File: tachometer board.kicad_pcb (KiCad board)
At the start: 2 copper layers, 22.4 x 13.5 mm, 5 parts, among them J1 Conn_01x04

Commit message: Update silkscreen and export gerbers
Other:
- board text added: "3.3VIN"
- board text added: "GND"
- board text added: "Nerf Tachometer Version 1.0 Designed by Mark Ghebrial"
- board text added: "OUT1"
- board text added: "OUT2"
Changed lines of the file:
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@@
     (descr "JST PH series connector, S4B-PH-K (http://www.jst-mfg.com/product/pdf/eng/ePH.pdf), generated with kicad-footprint-generator")
     (tags "connector JST PH top entry")
-    (property "Sheetfile" "protean board.kicad_sch")
+    (property "Sheetfile" "tachometer board.kicad_sch")
     (property "Sheetname" "")
     (property "ki_description" "Generic connector, single row, 01x04, script generated (kicad-library-utils/schlib/autogen/connector/)")
     (property "ki_keywords" "connector")
     (attr through_hole)
-    (fp_text reference "J1" (at 3 -2.55 180) (layer "F.SilkS")
+    (fp_text reference "J1" (at 3 -2.55 180) (layer "F.SilkS") hide
         (effects (font (size 1 1) (thickness 0.15)))
     )
@@
   (footprint "Marks Library:ITR20001-T" (layer "F.Cu")
     (at 164.067893 111.7 -90)
-    (property "Sheetfile" "protean board.kicad_sch")
+    (property "Sheetfile" "tachometer board.kicad_sch")
     (property "Sheetname" "")
     (attr through_hole)
@@
     (descr "Resistor SMD 1210 (3225 Metric), square (rectangular) end terminal, IPC_7351 nominal with elongated pad for handsoldering. (Body size source: IPC-SM-782 page 72, https://www.pcb-3d.com/wordpress/wp-content/uploads/ipc-sm-782a_amendment_1_and_2.pdf), generated with kicad-footprint-generator")
     (tags "resistor handsolder")
-    (property "Sheetfile" "protean board.kicad_sch")
+    (property "Sheetfile" "tachometer board.kicad_sch")
     (property "Sheetname" "")
     (property "ki_description" "Resistor")
@@
     (descr "Resistor SMD 1210 (3225 Metric), square (rectangular) end terminal, IPC_7351 nominal with elongated pad for handsoldering. (Body size source: IPC-SM-782 page 72, https://www.pcb-3d.com/wordpress/wp-content/uploads/ipc-sm-782a_amendment_1_and_2.pdf), generated with kicad-footprint-generator")
     (tags "resistor handsolder")
-    (property "Sheetfile" "protean board.kicad_sch")
+    (property "Sheetfile" "tachometer board.kicad_sch")
     (property "Sheetname" "")
     (property "ki_description" "Resistor")
@@
   (footprint "Marks Library:ITR20001-T" (layer "F.Cu")
     (at 148.317893 111.7 90)
-    (property "Sheetfile" "protean board.kicad_sch")
+    (property "Sheetfile" "tachometer board.kicad_sch")
     (property "Sheetname" "")
     (attr through_hole)
@@
   (gr_line (start 167.367893 114.242893) (end 167.367893 109.142893)
     (stroke (width 0.1) (type solid)) (layer "Edge.Cuts"))
+  (gr_text "3.3VIN" (at 159.85 101.19762 90) (layer "B.SilkS")
+    (effects (font (size 1 1) (thickness 0.15)) (justify left bottom mirror))
+  )
+  (gr_text "OUT2" (at 155.85 102.15 90) (layer "B.SilkS")
+    (effects (font (size 1 1) (thickness 0.15)) (justify left bottom mirror))
+  )
+  (gr_text "GND" (at 157.85 102.911905 90) (layer "B.SilkS")
+    (effects (font (size 1 1) (thickness 0.15)) (justify left bottom mirror))
+  )
+  (gr_text "Nerf Tachometer\nVersion 1.0\nDesigned by\nMark Ghebrial" (at 151.45 109.1 180) (layer "B.SilkS")
+    (effects (font (size 0.75 0.75) (thickness 0.15)) (justify left bottom mirror))
+  )
+  (gr_text "OUT1" (at 153.9 102.15 90) (layer "B.SilkS")
+    (effects (font (size 1 1) (thickness 0.15)) (justify left bottom mirror))
+  )
   (segment (start 159.192893 109.820711) (end 159.192893 107.15) (width 0.25) (layer "F.Cu") (net 1))
   (segment (start 154.934314 113.25) (end 153.4 113.25) (width 0.25) (layer "F.Cu") (net 1))

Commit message: Add README.md
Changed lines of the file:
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@@
       (outputformat 1)
       (mirror false)
-      (drillshape 1)
+      (drillshape 0)
       (scaleselection 1)
-      (outputdirectory "")
+      (outputdirectory "gerbers/")
     )
   )
@@
     (fp_line (start 7.95 6.25) (end 7.95 -1.35)
       (stroke (width 0.1) (type solid)) (layer "F.Fab"))
-    (pad "1" thru_hole roundrect (at 0 0 180) (size 1.2 1.75) (drill 0.75) (layers "*.Cu" "*.Mask") (roundrect_rratio 0.208333)
+    (pad "1" thru_hole roundrect (at 0 0 180) (size 1.2 1.75) (drill 0.75) (layers "*.Cu" "*.Mask") (roundrect_rratio 0.2083333333)
       (net 1 "+3.3V") (pinfunction "Pin_1") (pintype "passive"))
     (pad "2" thru_hole oval (at 2 0 180) (size 1.2 1.75) (drill 0.75) (layers "*.Cu" "*.Mask")
@@
     (fp_line (start 1.6 1.245) (end -1.6 1.245)
       (stroke (width 0.1) (type solid)) (layer "F.Fab"))
-    (pad "1" smd roundrect (at -1.55 0 90) (size 1.3 2.65) (layers "F.Cu" "F.Paste" "F.Mask") (roundrect_rratio 0.192308)
+    (pad "1" smd roundrect (at -1.55 0 90) (size 1.3 2.65) (layers "F.Cu" "F.Paste" "F.Mask") (roundrect_rratio 0.1923076923)
       (net 6 "Net-(U2-LED_VIN)") (pintype "passive"))
-    (pad "2" smd roundrect (at 1.55 0 90) (size 1.3 2.65) (layers "F.Cu" "F.Paste" "F.Mask") (roundrect_rratio 0.192308)
+    (pad "2" smd roundrect (at 1.55 0 90) (size 1.3 2.65) (layers "F.Cu" "F.Paste" "F.Mask") (roundrect_rratio 0.1923076923)
       (net 1 "+3.3V") (pintype "passive"))
     (model "${KICAD6_3DMODEL_DIR}/Resistor_SMD.3dshapes/R_1210_3225Metric.wrl"
@@
     (fp_line (start 1.6 1.245) (end -1.6 1.245)
       (stroke (width 0.1) (type solid)) (layer "F.Fab"))
-    (pad "1" smd roundrect (at -1.55 0 270) (size 1.3 2.65) (layers "F.Cu" "F.Paste" "F.Mask") (roundrect_rratio 0.192308)
+    (pad "1" smd roundrect (at -1.55 0 270) (size 1.3 2.65) (layers "F.Cu" "F.Paste" "F.Mask") (roundrect_rratio 0.1923076923)
       (net 5 "Net-(U1-LED_VIN)") (pintype "passive"))
-    (pad "2" smd roundrect (at 1.55 0 270) (size 1.3 2.65) (layers "F.Cu" "F.Paste" "F.Mask") (roundrect_rratio 0.192308)
+    (pad "2" smd roundrect (at 1.55 0 270) (size 1.3 2.65) (layers "F.Cu" "F.Paste" "F.Mask") (roundrect_rratio 0.1923076923)
       (net 1 "+3.3V") (pintype "passive"))
     (model "${KICAD6_3DMODEL_DIR}/Resistor_SMD.3dshapes/R_1210_3225Metric.wrl"
@@
     (effects (font (size 1 1) (thickness 0.15)) (justify left bottom mirror))
   )
-  (gr_text "Nerf Tachometer\nVersion 1.0\nDesigned by\nMark Ghebrial" (at 151.45 109.1 180) (layer "B.SilkS")
-    (effects (font (size 0.75 0.75) (thickness 0.15)) (justify left bottom mirror))
-  )
-  (gr_text "OUT1" (at 153.9 102.15 90) (layer "B.SilkS")
+  (gr_text "Nerf Tachometer\nVersion 1.0\nDesigned by\nMark Ghebrial" (at 151.45 108.8 180) (layer "B.SilkS")
+    (effects (font (size 0.8 0.75) (thickness 0.15)) (justify left bottom mirror))
+  )
+  (gr_text "OUT1" (at 153.85 102.15 90) (layer "B.SilkS")
     (effects (font (size 1 1) (thickness 0.15)) (justify left bottom mirror))
   )

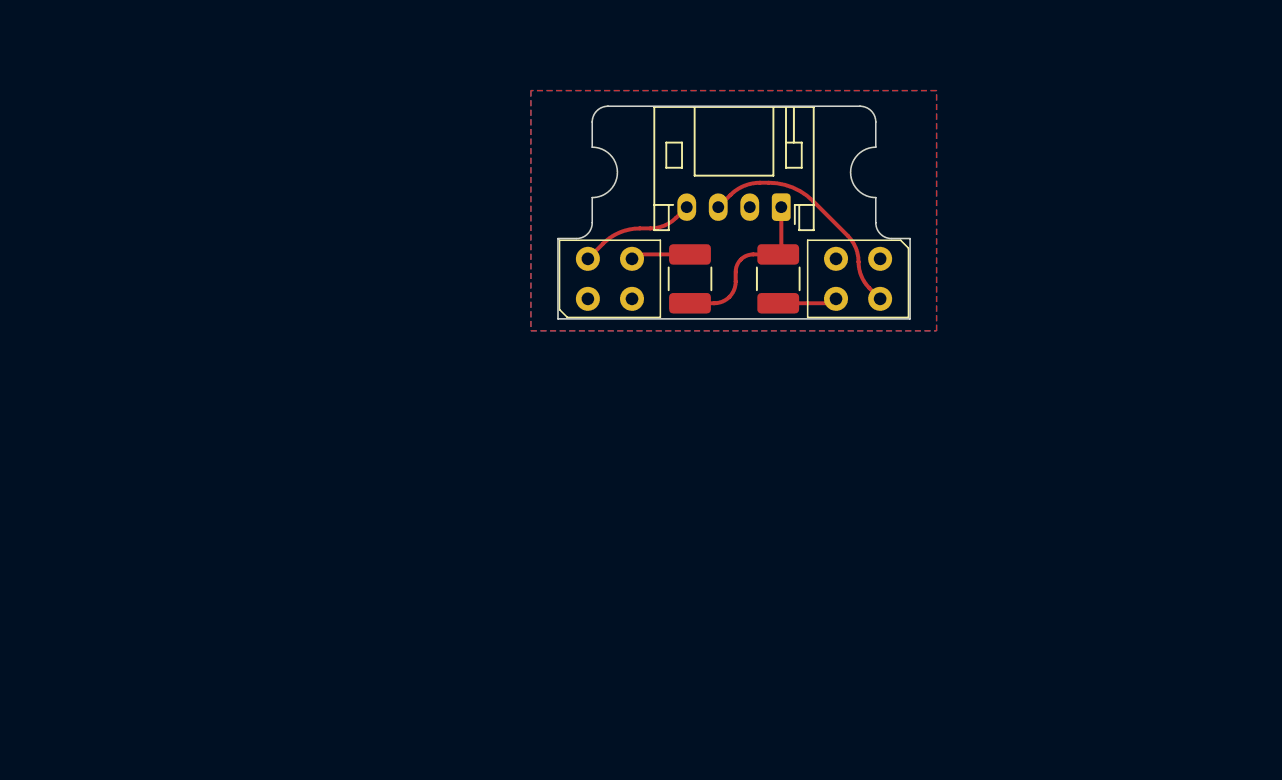
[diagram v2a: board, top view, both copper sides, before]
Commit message: Add SAMD MCU and MOSFET
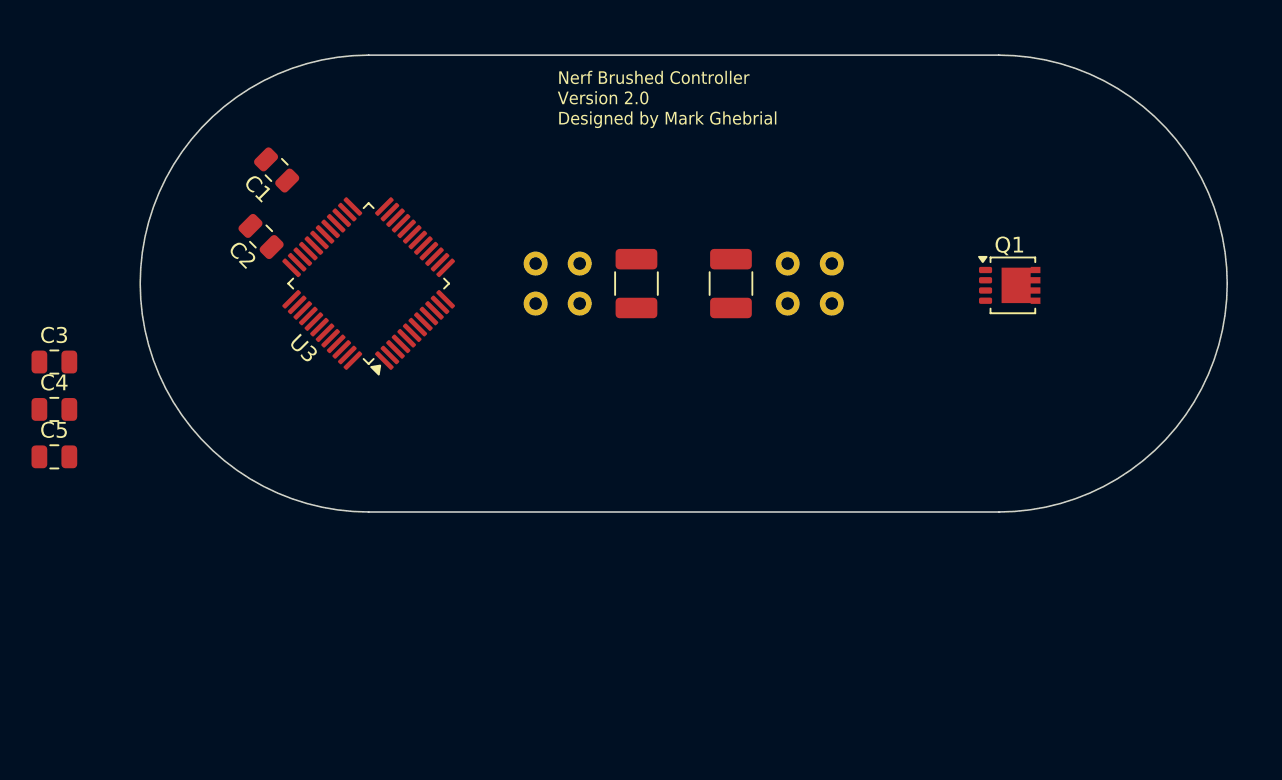
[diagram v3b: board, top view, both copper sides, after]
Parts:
- removed J1: Conn_01x04, Connector_JST:JST_PH_S4B-PH-K_1x04_P2.00mm_Horizontal
- added C1: C, Capacitor_SMD:C_0805_2012Metric, F.Cu at (127.2, 104.8)
- added C2: C, Capacitor_SMD:C_0805_2012Metric, F.Cu at (126.2, 109.0)
- added C3: C, Capacitor_SMD:C_0805_2012Metric, F.Cu at (113.0, 117.0)
- added C4: C, Capacitor_SMD:C_0805_2012Metric, F.Cu at (113.0, 120.0)
- added C5: C, Capacitor_SMD:C_0805_2012Metric, F.Cu at (113.0, 123.0)
- added Q1: PSMN8R5-40MSDX, Package_TO_SOT_SMD:LFPAK33, F.Cu at (173.7, 112.1)
- added U3: ATSAMD21G18A-A, Package_QFP:TQFP-48_7x7mm_P0.5mm, F.Cu at (133.0, 112.0)
- U1, U2: moved to B.Cu
- moved U2 19.1 mm to (145.0, 112.0)
- moved U1 12.7 mm to (161.0, 112.0)
- moved R1 3.41 mm to (150.0, 112.0)
- moved R2 3.01 mm to (156.0, 112.0)
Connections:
- U1 pad 4: /OUT1 -> /TACHA
- U2 pad 4: /OUT2 -> /TACHB
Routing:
- net /OUT2: track 14.6 -> 0.00 mm
- net +3.3V: track 10.7 -> 0.00 mm
- net /OUT1: track 7.36 -> 0.00 mm
- net Net-(U1-LED_VIN): track 3.78 -> 0.00 mm
- net Net-(U2-LED_VIN): track 3.76 -> 0.00 mm
- removed copper zone on B.Cu, net GND
- removed copper zone on F.Cu, net GND
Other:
- board size 22.4 x 13.5 mm -> 69 x 29 mm
- board text added: "Nerf Brushed Controller Version 2.0 Designed by Mark Ghebrial"
- board text removed: "3.3VIN"
- board text removed: "GND"
- board text removed: "Nerf Tachometer Version 1.0 Designed by Mark Ghebrial"
- board text removed: "OUT1"
- board text removed: "OUT2"

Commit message: Misc. changes to schematic and PCB
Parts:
- added J1: USB_B_Micro, Connector_USB:USB_Micro-B_Molex_47346-0001, F.Cu at (137.0, 100.5)
- added J2: Conn_01x05_Pin, Marks Library:4mm_by_6mm_Solder_Pad_x5, F.Cu at (165.0, 138.5)
- added Q2: PSMN8R5-40MSX, Package_TO_SOT_SMD:LFPAK33, F.Cu at (144.3, 133.2)
- added REF**: AMASS_XT30PW-F_1x02_P2.50mm_Horizontal, Connector_AMASS:AMASS_XT30PW-F_1x02_P2.50mm_Horizontal, B.Cu at (173.2, 107.5)
- added REF**: AMASS_XT30PW-M_1x02_P2.50mm_Horizontal, Connector_AMASS:AMASS_XT30PW-M_1x02_P2.50mm_Horizontal, B.Cu at (156.0, 116.8)
- added REF**: AMASS_XT30PW-F_1x02_P2.50mm_Horizontal, Connector_AMASS:AMASS_XT30PW-F_1x02_P2.50mm_Horizontal, B.Cu at (173.2, 121.2)
- added U4: ZXGD3009DY, Package_TO_SOT_SMD:SOT-23-6, F.Cu at (153.2, 133.2)
- added U5: ZXGD3009DY, Package_TO_SOT_SMD:SOT-23-6, F.Cu at (148.8, 133.2)
- added U6: AP2112K-3.3, Package_TO_SOT_SMD:SOT-23-5, F.Cu at (146.4, 105.5)
- C1, C2, C3, C4: footprint Capacitor_SMD:C_0805_2012Metric -> Capacitor_SMD:C_0402_1005Metric
- C5: value C -> 1uF; footprint Capacitor_SMD:C_0805_2012Metric -> Capacitor_SMD:C_0402_1005Metric
- Q1: value PSMN8R5-40MSDX -> PSMN8R5-40MSX
- moved Q1 26.5 mm to (157.7, 133.2)
- moved C5 19.2 mm to (126.6, 109.3), turned to 135 degrees
- moved C4 18.8 mm to (127.8, 108.2), turned to 135 degrees
- moved C3 18.5 mm to (128.8, 107.2), turned to 135 degrees
- moved C1 12.8 mm to (126.3, 117.6)
- moved C2 7.22 mm to (128.0, 116.0)
- moved R1 6.00 mm to (156.0, 112.0)
- moved R2 6.00 mm to (150.0, 112.0)
- turned U3 to 45 degrees
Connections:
- C5 pad 1: +3V3 -> Net-(U3-VDDCORE)
- Q1 pad 1: Net-(Q1-S-Pad1) -> GND
- Q1 pad 2: Net-(Q1-S-Pad1) -> GND
- Q1 pad 3: Net-(Q1-S-Pad1) -> GND
- Q1 pad 4: unconnected-(Q1-G-Pad4) -> /GATEA
- Q1 pad 5: unconnected-(Q1-D-Pad5) -> MOTORA-
- U1 pad 4: /TACHA -> TACHA
- U2 pad 4: /TACHB -> TACHB
- U3 pad 18: Net-(U3-GND-Pad18) -> GND
- U3 pad 25: unconnected-(U3-PA16-Pad25) -> TACHB
- U3 pad 26: unconnected-(U3-PA17-Pad26) -> TACHA
- U3 pad 33: unconnected-(U3-PA24-Pad33) -> USB_D-
- U3 pad 34: unconnected-(U3-PA25-Pad34) -> USB_D+
- U3 pad 35: Net-(U3-GND-Pad18) -> GND
- U3 pad 40: unconnected-(U3-~{RESET}-Pad40) -> RESET
- U3 pad 42: Net-(U3-GND-Pad18) -> GND
- U3 pad 43: +3V3 -> Net-(U3-VDDCORE)
- U3 pad 5: unconnected-(U3-GNDANA-Pad5) -> GND
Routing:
- net TACHA: track 0.00 -> 26.4 mm
- net USB_D-: track 0.00 -> 7.25 mm
- net TACHB: track 0.00 -> 7.07 mm
- net USB_D+: track 0.00 -> 6.87 mm
- net Net-(U2-LED_VIN): track 0.00 -> 3.72 mm
- net Net-(U1-LED_VIN): track 0.00 -> 3.72 mm
- added copper zone on F.Cu, net GND

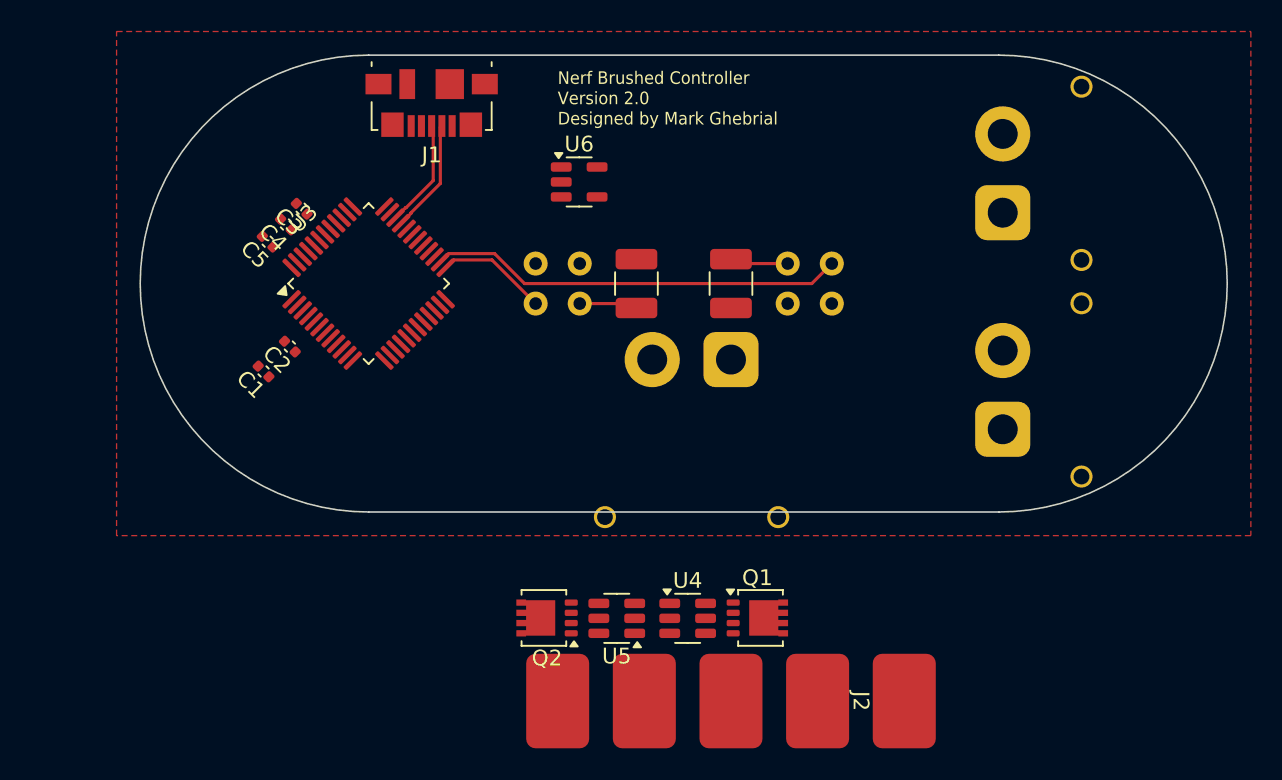
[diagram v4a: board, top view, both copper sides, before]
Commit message: Add buck converter
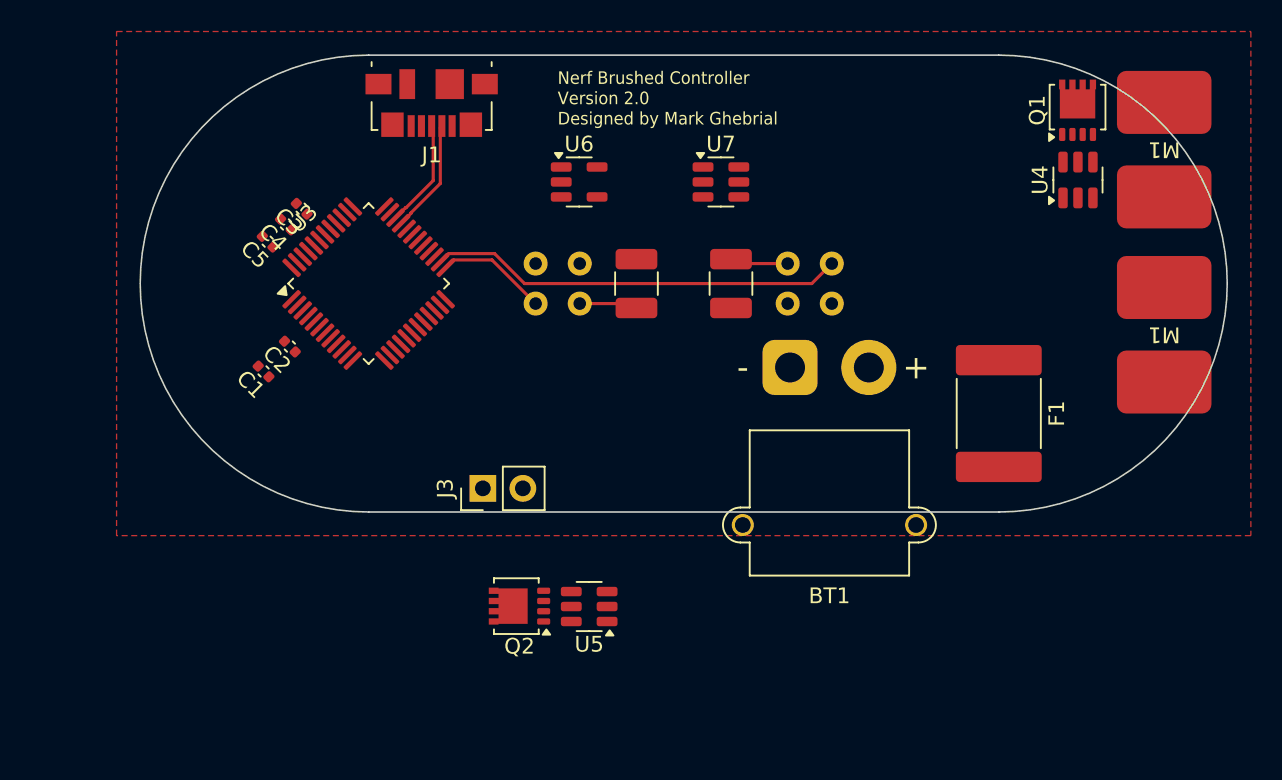
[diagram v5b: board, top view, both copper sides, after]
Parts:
- removed J2: Conn_01x05_Pin, Marks Library:4mm_by_6mm_Solder_Pad_x5
- removed REF** (x2): AMASS_XT30PW-F_1x02_P2.50mm_Horizontal, Connector_AMASS:AMASS_XT30PW-F_1x02_P2.50mm_Horizontal
- removed REF**: AMASS_XT30PW-M_1x02_P2.50mm_Horizontal, Connector_AMASS:AMASS_XT30PW-M_1x02_P2.50mm_Horizontal
- added BT1: Battery, Connector_AMASS:AMASS_XT30PW-M_1x02_P2.50mm_Horizontal, F.Cu at (159.8, 117.3)
- added F1: 5A, Fuse:Fuse_2920_7451Metric, F.Cu at (173.0, 120.2)
- added J3: Conn_01x02_Pin, Connector_PinHeader_2.54mm:PinHeader_1x02_P2.54mm_Vertical, F.Cu at (140.2, 125.0)
- added M1: Motor_DC, Marks Library:4mm_by_6mm_Solder_Pad_x2, F.Cu at (183.5, 116.2)
- added M1: Motor_DC, Marks Library:4mm_by_6mm_Solder_Pad_x2, F.Cu at (183.5, 104.5)
- added U7: AP62250WU, Package_TO_SOT_SMD:TSOT-23-6, F.Cu at (155.4, 105.5)
- moved Q1 38.1 mm to (178.0, 101.0), turned to 90 degrees
- moved U4 37.3 mm to (178.0, 105.4), turned to 90 degrees
- moved Q2 1.90 mm to (142.6, 132.5)
- moved U5 1.90 mm to (147.0, 132.5)
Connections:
- net Net-(U6-VIN) renamed +5V
- net RESET renamed Net-(U3-~{RESET})
- Q1 pad 5: MOTORA- -> Net-(M1--)

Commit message: Misc changes
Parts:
- added C10: 470uF, Capacitor_SMD:CP_Elec_8x10, F.Cu at (167.0, 103.2)
